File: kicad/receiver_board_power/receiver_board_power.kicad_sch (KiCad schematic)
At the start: 5 parts, among them J1 Battery Conn, Q1 FQP27P06, U1 2S BMS, U2 5V Buck

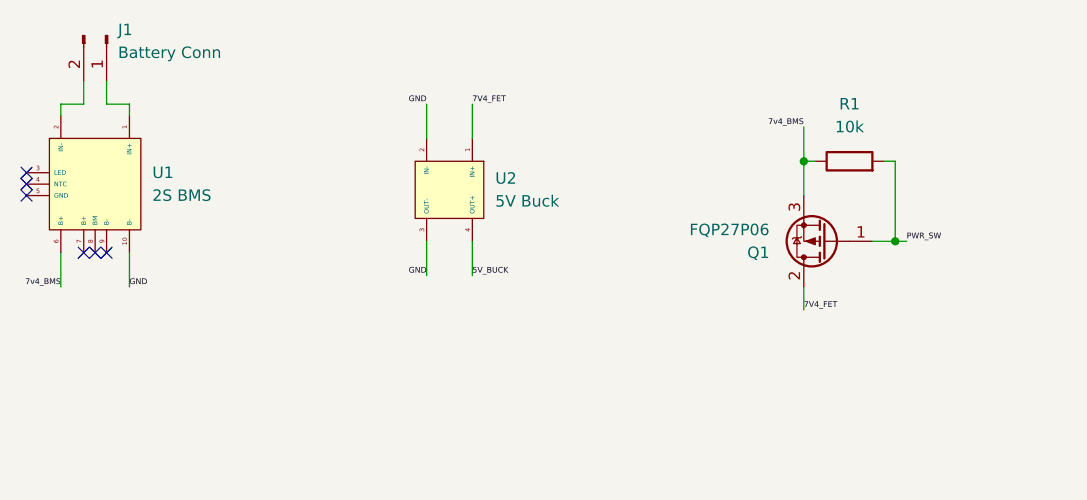
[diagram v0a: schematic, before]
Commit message: Finished generating footprints for all parts. Receiver boards layout and stacking order is still TBD, so renamed them from "uppper" and "lower" to "power" and "logic" as that will likely be the rough distribution of parts between them.
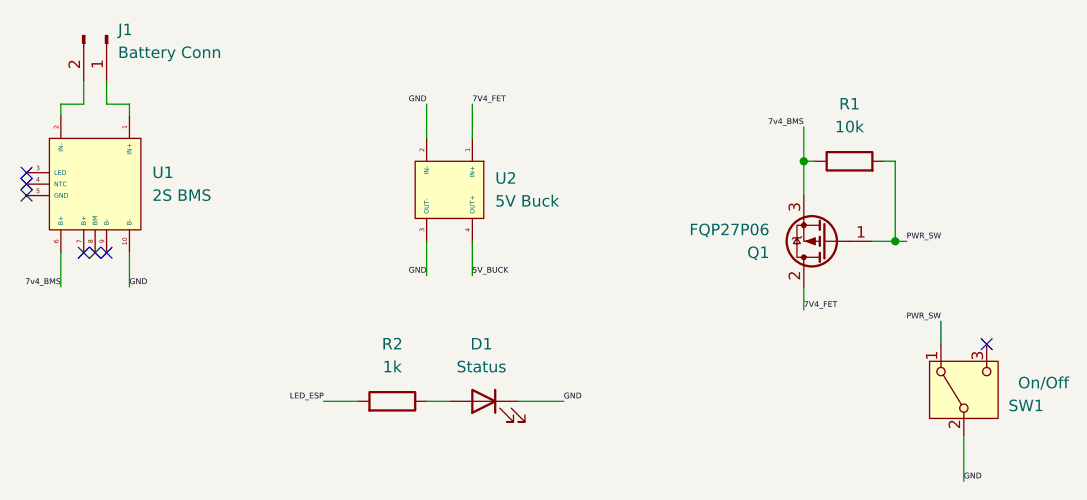
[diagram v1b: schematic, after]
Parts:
- added D1: Status, LED_THT:LED_D5.0mm, symbol Device:LED
- added R2: 1k, Resistor_THT:R_Axial_DIN0207_L6.3mm_D2.5mm_P7.62mm_Horizontal, symbol Device:R
- added SW1: On/Off, ESP32_Lego_PF:Slide_Switch_SPDT_12D00G, symbol Switch:SW_SPDT
- U1: footprint (none) -> ESP32_Lego_PF:2S BMS
- U2: footprint (none) -> ESP32_Lego_PF:MP1584EN
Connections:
- net GND: now also D1.1 (K), SW1.2 (B)
- net PWR_SW: now also SW1.1 (A)
- new net: D1.2 (A), R2.1
- new net LED_ESP: R2.2
- no-connect marks 6 -> 7
